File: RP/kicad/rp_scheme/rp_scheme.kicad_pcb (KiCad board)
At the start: 2 copper layers, 42 x 40.2 mm, 28 parts, among them J1 Screw_Terminal_01x06, J2 Conn_02x03_Odd_Even, K1 Relay_SPST_Latching_2coil, Q1 2N7000, Q2 2N7000, SW1 SW_Push, U1 NRF24L01_Breakout, U2 AMS1117-3.3, U3 STM32F103C6Tx

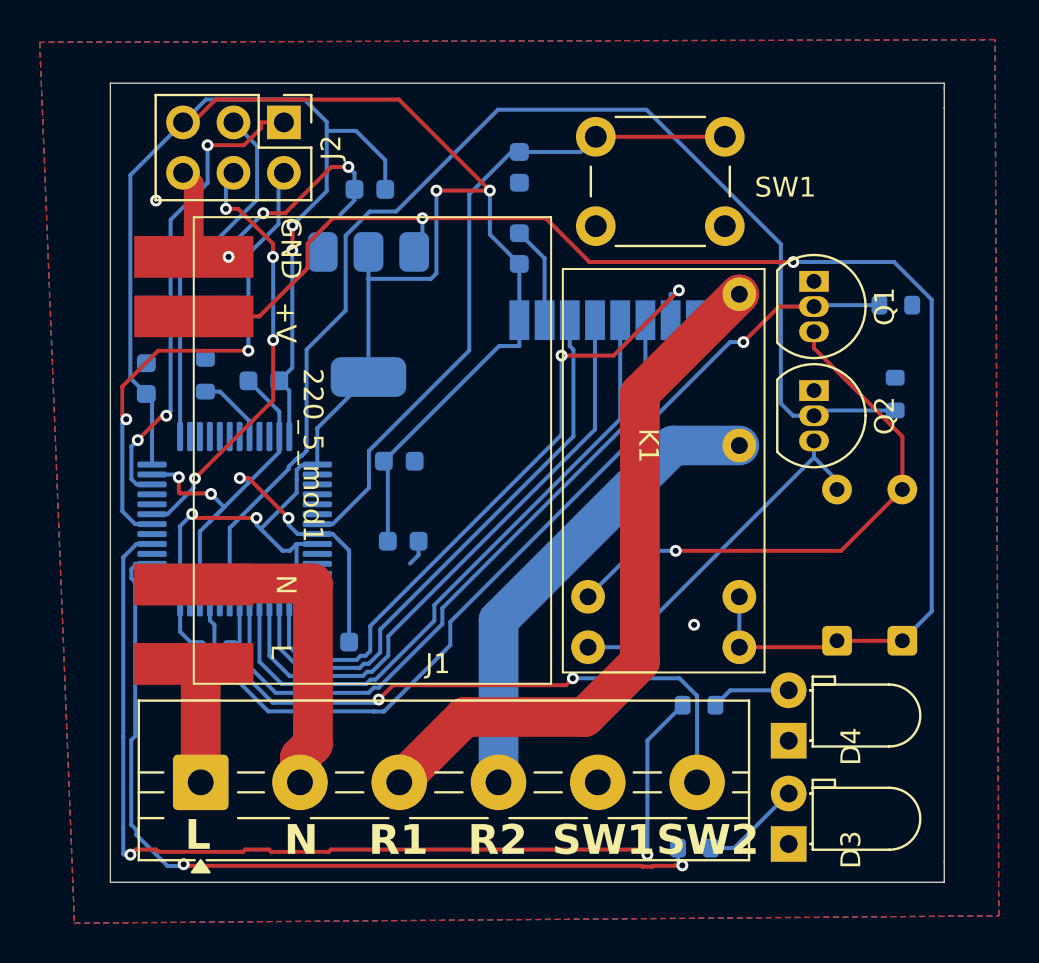
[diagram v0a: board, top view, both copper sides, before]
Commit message: РП: изменены габариты платы
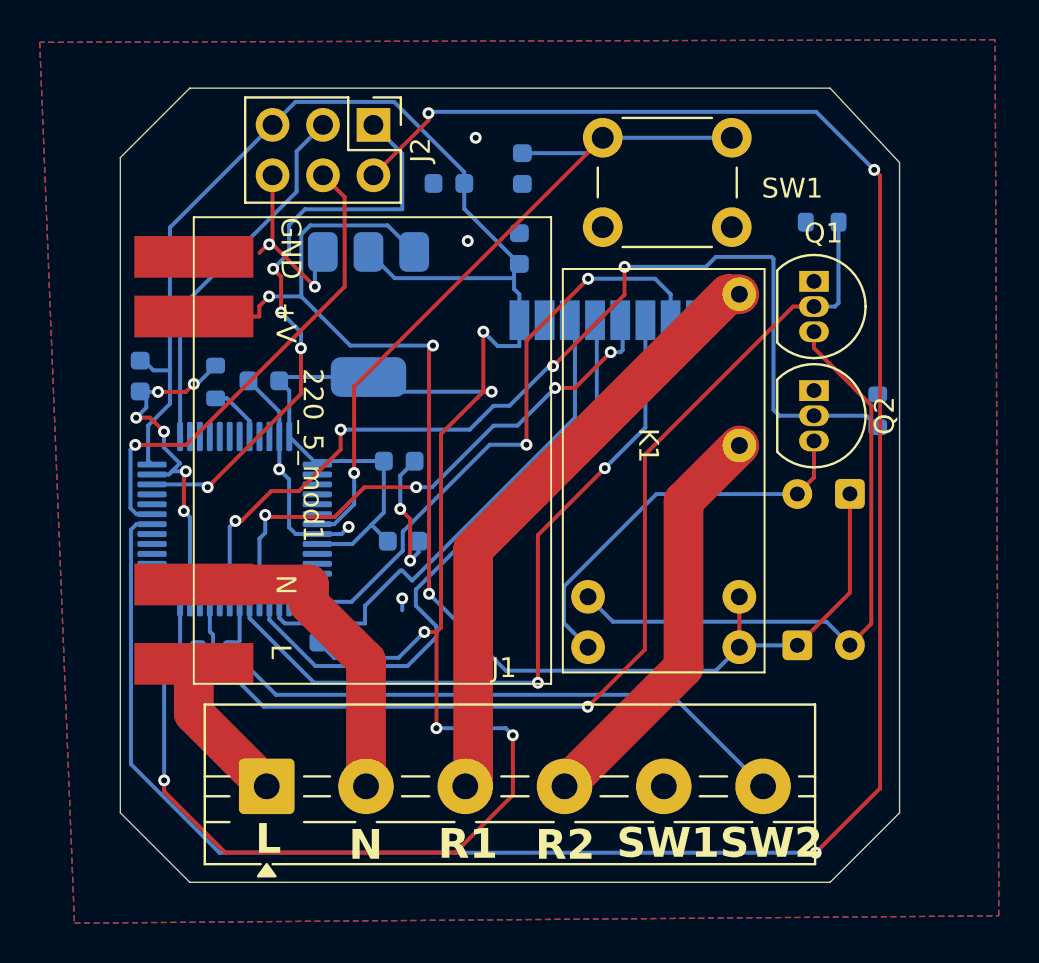
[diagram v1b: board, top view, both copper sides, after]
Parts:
- removed D3: R_LED, LED_THT:LED_D3.0mm_Horizontal_O1.27mm_Z2.0mm
- removed D4: G_LED, LED_THT:LED_D3.0mm_Horizontal_O1.27mm_Z2.0mm
- removed R4, R5: 270, Resistor_SMD:R_0603_1608Metric
- moved D2 7.86 mm to (149.2, 100.4), turned to -90 degrees
- moved R1 5.59 mm to (147.8, 86.8), turned to 180 degrees
- moved J2 4.51 mm to (125.2, 81.8)
- moved C2 3.99 mm to (129.1, 84.8)
- moved J1 3.33 mm to (119.9, 115.2)
- moved D1 2.01 mm to (146.6, 108.1)
- moved R2 1.22 mm to (150.7, 96.2)
- moved R6 0.61 mm to (117.3, 94.8)
- moved SW1 0.35 mm to (143.3, 87.0)
- moved C3 0.34 mm to (113.5, 94.5), turned to -90 degrees
- moved C1 0.16 mm to (132.8, 84.0)
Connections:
- U3 pad 26: Net-(U3-PB13) -> unconnected-(U3-PB13-Pad26)
- U3 pad 28: Net-(U3-PB15) -> unconnected-(U3-PB15-Pad28)
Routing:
- net /TX: track 25.0 -> 113.1 mm, vias 2 -> 3
- net Net-(U3-PB15): track 51.8 -> 0.00 mm, vias 2 -> 0
- net Net-(U3-PB13): track 44.2 -> 0.00 mm, vias 2 -> 0
- net /SET_PIN: track 62.6 -> 51.5 mm, vias 0 -> 4
- net +3V3: track 136.0 -> 146.6 mm
- net Earth: track 56.2 -> 47.0 mm, vias 9 -> 15
- net /RST_PIN: track 46.7 -> 53.6 mm
- net /SWDIO: track 24.2 -> 29.8 mm, vias 3 -> 4
- net Net-(D3-A): track 5.06 -> 0.00 mm
- net /SCK: track 32.6 -> 27.6 mm, vias 0 -> 4
- net /R1: track 35.2 -> 30.8 mm
- net +5V: track 72.2 -> 67.9 mm, vias 2 -> 3
- net Net-(D4-A): track 4.00 -> 0.00 mm
- net /R_reset: track 27.9 -> 31.6 mm, vias 1 -> 0
- net /MISO: track 34.8 -> 31.2 mm
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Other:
- board size 42 x 40.2 mm -> 39.2 x 40 mm
